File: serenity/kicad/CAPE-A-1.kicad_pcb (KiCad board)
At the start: 4 copper layers, 55 x 35 mm, 25 parts

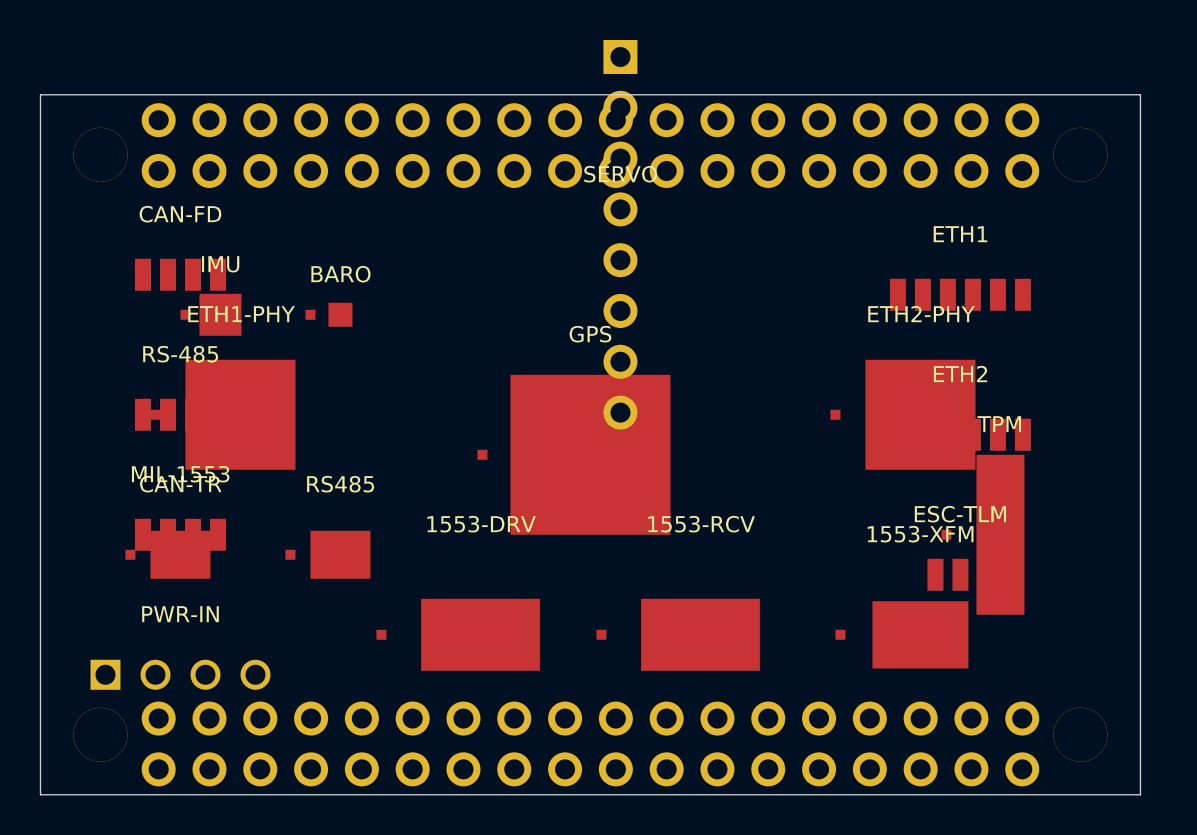
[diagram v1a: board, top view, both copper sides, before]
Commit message: Add back-side RF/storage to CAPE-A-1; add GPIO expansion headers to CAPE-B-1
CAPE-A-1.kicad_pcb:
- Move RFM95W LoRa, WL1837MOD WiFi/BT, ATF16V8BQL CPLD write-blocker,
  W25Q128JV NOR flash, and microSD log slot to B.Cu back side
- Add nets for SPI1 bus (LoRa/NOR), SDIO bus (WiFi), and SD card signals
- Update title comment to list front/back component inventory

CAPE-B-1.kicad_pcb:
- Add 6 × JST-GH 3-pin GPIO expansion connectors (GPIO-A through GPIO-F)
  along bottom edge at 7mm spacing
- Add nets GPIO_EXP_A through GPIO_EXP_F
- Update title comment to mention GPIO expansion

https://claude.ai/code/session_01GniMw4QukTVM7JMzyVjH6p
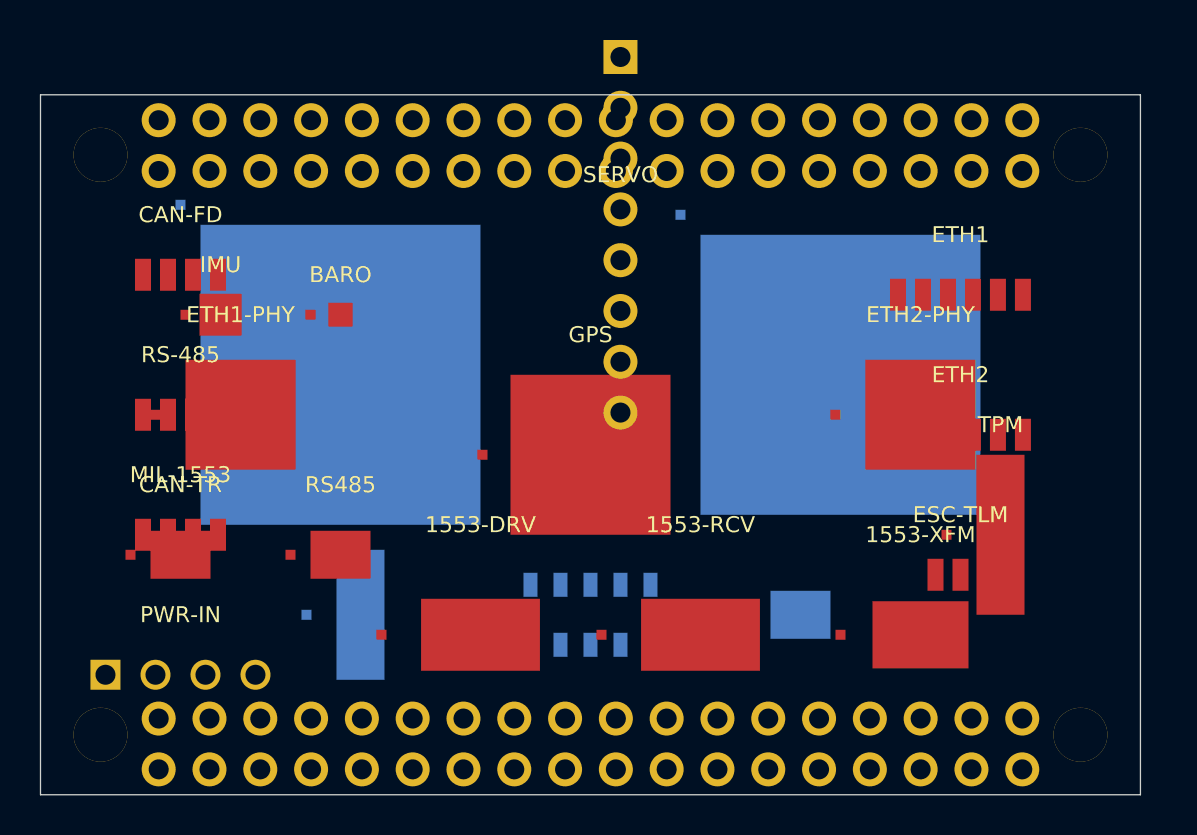
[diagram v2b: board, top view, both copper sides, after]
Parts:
- added J_SD: microSD-Log, microSD_Slot, B.Cu at (148.5, 113.5)
- added LORA: RFM95W, RF_Module, B.Cu at (136.0, 101.5)
- added NOR-FLASH: W25Q128JV, Package, B.Cu at (159.0, 113.5)
- added SD-WB: ATF16V8BQL, Package, B.Cu at (137.0, 113.5)
- added WIFI-BT: WL1837MOD, RF_Module, B.Cu at (161.0, 101.5)
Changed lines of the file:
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@@
     (comment 2 "CC BY 4.0 creativecommons.org/licenses/by/4.0")
     (comment 3 "PocketBeagle 2 Industrial (AM6254) expansion — 55x35mm 4L JLCPCB assembled")
-    (comment 4 "ICM-42688-P IMU | BMP388 Baro | SAM-M10Q GPS | ATA6561 CAN FD | MAX3485E RS-485 | DS26LV31/32 1553 | DP83825I x2 ETH | SLB9670 TPM2")
+    (comment 4 "F: ICM-42688-P IMU | BMP388 Baro | SAM-M10Q GPS | ATA6561 CAN FD | MAX3485E RS-485 | DS26LV31/32 1553 | DP83825I x2 ETH | SLB9670 TPM2 | B: RFM95W LoRa | WL1837MOD WiFi/BT | ATF16V8BQL CPLD | W25Q128JV NOR | microSD log slot")
     (comment 5 "Hull: Peter Farell CC BY 4.0 | Nozzle: BamJr CC BY 4.0 | Firefly/Serenity fan-work, not officially licensed")
   )
@@
   (net 84 "ETH2_RX_P")
   (net 85 "ETH2_RX_N")
+  (net 86 "SPI1_CLK")
+  (net 87 "SPI1_MOSI")
+  (net 88 "SPI1_MISO")
+  (net 89 "SPI1_CS_LORA")
+  (net 90 "SPI1_CS_NOR")
+  (net 91 "LORA_DIO0")
+  (net 92 "LORA_RESETN")
+  (net 93 "SDIO_CLK")
+  (net 94 "SDIO_CMD")
+  (net 95 "SDIO_D0")
+  (net 96 "SDIO_D1")
+  (net 97 "SDIO_D2")
+  (net 98 "SDIO_D3")
+  (net 99 "WL_EN")
+  (net 100 "SD_CLK")
+  (net 101 "SD_CMD")
+  (net 102 "SD_D0")
+  (net 103 "SD_D1")
+  (net 104 "SD_D2")
+  (net 105 "SD_D3")
+  (net 106 "SD_CD")
   (gr_line (start 121 87.5) (end 176 87.5) (layer "Edge.Cuts") (width 0.05))
   (gr_line (start 176 87.5) (end 176 122.5) (layer "Edge.Cuts") (width 0.05))
@@
     (pad "3" thru_hole circle (at 1.25 0) (size 1.5 1.5) (drill 1.0) (layers "*.Cu" "*.Mask"))
     (pad "4" thru_hole circle (at 3.75 0) (size 1.5 1.5) (drill 1.0) (layers "*.Cu" "*.Mask")))
+  (footprint "RF_Module" (layer "B.Cu") (at 136 101.5) (property "Description" "Hope RFM95W LoRa 868/915MHz SPI module 16x17mm — back side, SPI1")
+    (fp_text reference "LORA" (at 0 -10) (layer "B.SilkS")
+      (effects (font (size 0.8 0.8) (thickness 0.15)) (justify mirror)))
+    (fp_text value "RFM95W" (at 0 10) (layer "B.Fab")
+      (effects (font (size 0.8 0.8) (thickness 0.15)) (justify mirror)))
+    (fp_poly (pts (xy -8.0 -8.5) (xy 8.0 -8.5) (xy 8.0 8.5) (xy -8.0 8.5))
+     (layer "B.CrtYd") (width 0.05))
+    (pad "1" smd rect (at -8.0 -8.5) (size 0.5 0.5) (layers "B.Cu" "B.Paste" "B.Mask"))
+    (pad "EP" smd rect (at 0 0) (size 14.0 15.0) (layers "B.Cu" "B.Paste" "B.Mask")))
+  (footprint "RF_Module" (layer "B.Cu") (at 161 101.5) (property "Description" "TI WL1837MOD WiFi 802.11bgn BT4.0 SDIO module 16x16mm — back side, SDIO")
+    (fp_text reference "WIFI-BT" (at 0 -10) (layer "B.SilkS")
+      (effects (font (size 0.8 0.8) (thickness 0.15)) (justify mirror)))
+    (fp_text value "WL1837MOD" (at 0 10) (layer "B.Fab")
+      (effects (font (size 0.8 0.8) (thickness 0.15)) (justify mirror)))
+    (fp_poly (pts (xy -8.0 -8.0) (xy 8.0 -8.0) (xy 8.0 8.0) (xy -8.0 8.0))
+     (layer "B.CrtYd") (width 0.05))
+    (pad "1" smd rect (at -8.0 -8.0) (size 0.5 0.5) (layers "B.Cu" "B.Paste" "B.Mask"))
+    (pad "EP" smd rect (at 0 0) (size 14.0 14.0) (layers "B.Cu" "B.Paste" "B.Mask")))
+  (footprint "Package" (layer "B.Cu") (at 137 113.5) (property "Description" "Microchip ATF16V8BQL GAL CPLD write-blocker for microSD TSSOP-24 — back side")
+    (fp_text reference "SD-WB" (at 0 -4.5) (layer "B.SilkS")
+      (effects (font (size 0.8 0.8) (thickness 0.15)) (justify mirror)))
+    (fp_text value "ATF16V8BQL" (at 0 4.5) (layer "B.Fab")
+      (effects (font (size 0.8 0.8) (thickness 0.15)) (justify mirror)))
+    (fp_poly (pts (xy -2.70 -4.15) (xy 2.70 -4.15) (xy 2.70 4.15) (xy -2.70 4.15))
+     (layer "B.CrtYd") (width 0.05))
+    (pad "1" smd rect (at -2.70 0) (size 0.5 0.5) (layers "B.Cu" "B.Paste" "B.Mask"))
+    (pad "EP" smd rect (at 0 0) (size 2.40 6.50) (layers "B.Cu" "B.Paste" "B.Mask")))
+  (footprint "Package" (layer "B.Cu") (at 159 113.5) (property "Description" "Winbond W25Q128JV 128Mbit NOR flash SPI SOIC-8 — back side, SPI1")
+    (fp_text reference "NOR-FLASH" (at 0 -3.5) (layer "B.SilkS")
+      (effects (font (size 0.8 0.8) (thickness 0.15)) (justify mirror)))
+    (fp_text value "W25Q128JV" (at 0 3.5) (layer "B.Fab")
+      (effects (font (size 0.8 0.8) (thickness 0.15)) (justify mirror)))
+    (fp_poly (pts (xy -2.50 -2.00) (xy 2.50 -2.00) (xy 2.50 2.00) (xy -2.50 2.00))
+     (layer "B.CrtYd") (width 0.05))
+    (pad "1" smd rect (at -2.50 0) (size 0.5 0.5) (layers "B.Cu" "B.Paste" "B.Mask"))
+    (pad "EP" smd rect (at 0 0) (size 3.00 2.40) (layers "B.Cu" "B.Paste" "B.Mask")))
+  (footprint "microSD_Slot" (layer "B.Cu") (at 148.5 113.5) (property "Description" "microSD push-push slot for write-blocked log storage — back side, Molex 503182-1853 or equiv")
+    (fp_text reference "J_SD" (at 0 -4) (layer "B.SilkS")
+      (effects (font (size 0.8 0.8) (thickness 0.15)) (justify mirror)))
+    (fp_text value "microSD-Log" (at 0 4) (layer "B.Fab")
+      (effects (font (size 0.8 0.8) (thickness 0.15)) (justify mirror)))
+    (fp_poly (pts (xy -7.5 -2.0) (xy 7.5 -2.0) (xy 7.5 2.0) (xy -7.5 2.0))
+     (layer "B.CrtYd") (width 0.05))
+    (pad "1" smd rect (at -3.0 -1.5) (size 0.7 1.2) (layers "B.Cu" "B.Paste" "B.Mask"))
+    (pad "2" smd rect (at -1.5 -1.5) (size 0.7 1.2) (layers "B.Cu" "B.Paste" "B.Mask"))
+    (pad "3" smd rect (at 0.0 -1.5) (size 0.7 1.2) (layers "B.Cu" "B.Paste" "B.Mask"))
+    (pad "4" smd rect (at 1.5 -1.5) (size 0.7 1.2) (layers "B.Cu" "B.Paste" "B.Mask"))
+    (pad "5" smd rect (at 3.0 -1.5) (size 0.7 1.2) (layers "B.Cu" "B.Paste" "B.Mask"))
+    (pad "6" smd rect (at -3.0 1.5) (size 0.7 1.2) (layers "B.Cu" "B.Paste" "B.Mask"))
+    (pad "7" smd rect (at -1.5 1.5) (size 0.7 1.2) (layers "B.Cu" "B.Paste" "B.Mask"))
+    (pad "8" smd rect (at 0.0 1.5) (size 0.7 1.2) (layers "B.Cu" "B.Paste" "B.Mask"))
+    (pad "9" smd rect (at 1.5 1.5) (size 0.7 1.2) (layers "B.Cu" "B.Paste" "B.Mask"))
+    (pad "10" smd rect (at 3.0 1.5) (size 0.7 1.2) (layers "B.Cu" "B.Paste" "B.Mask")))
 )

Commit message: Correct placement: flip RF/storage to B.Cu on CAPE-B-1; revert CAPE-A-1
CAPE-B-1.kicad_pcb:
- Flip existing RFM95W LoRa, WL1837MOD WiFi/BT, ATF16V8BQL CPLD
  write-blocker, W25Q128JV NOR flash, and microSD log slot from F.Cu
  to B.Cu (layer, silk, fab, courtyard, pad layers, justify mirror)
- Update title comment to distinguish F/B component inventory

CAPE-A-1.kicad_pcb:
- Revert erroneously added back-side RF/storage footprints and nets
- Restore original title comment (front-only sensor/comms cape)

https://claude.ai/code/session_01GniMw4QukTVM7JMzyVjH6p
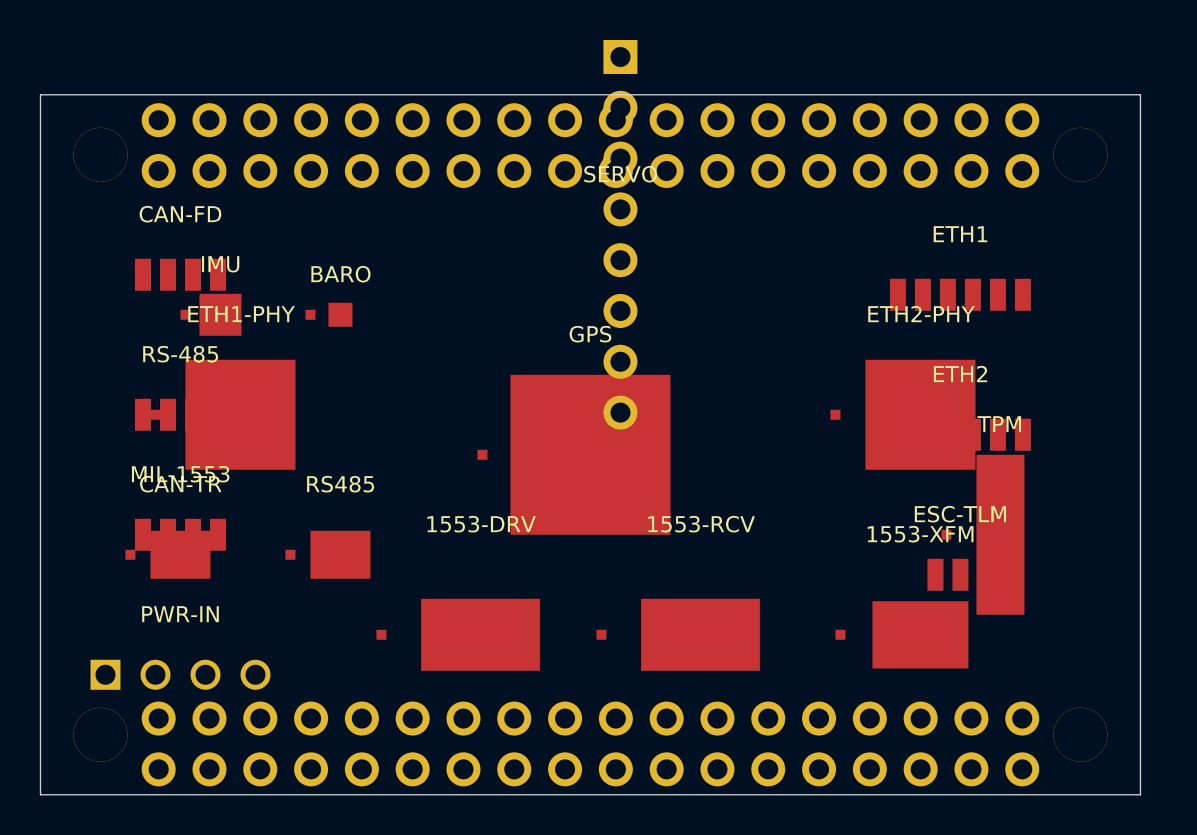
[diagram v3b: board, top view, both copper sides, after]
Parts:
- removed J_SD: microSD-Log, microSD_Slot
- removed LORA: RFM95W, RF_Module
- removed NOR-FLASH: W25Q128JV, Package
- removed SD-WB: ATF16V8BQL, Package
- removed WIFI-BT: WL1837MOD, RF_Module
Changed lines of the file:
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@@
     (comment 2 "CC BY 4.0 creativecommons.org/licenses/by/4.0")
     (comment 3 "PocketBeagle 2 Industrial (AM6254) expansion — 55x35mm 4L JLCPCB assembled")
-    (comment 4 "F: ICM-42688-P IMU | BMP388 Baro | SAM-M10Q GPS | ATA6561 CAN FD | MAX3485E RS-485 | DS26LV31/32 1553 | DP83825I x2 ETH | SLB9670 TPM2 | B: RFM95W LoRa | WL1837MOD WiFi/BT | ATF16V8BQL CPLD | W25Q128JV NOR | microSD log slot")
+    (comment 4 "ICM-42688-P IMU | BMP388 Baro | SAM-M10Q GPS | ATA6561 CAN FD | MAX3485E RS-485 | DS26LV31/32 1553 | DP83825I x2 ETH | SLB9670 TPM2")
     (comment 5 "Hull: Peter Farell CC BY 4.0 | Nozzle: BamJr CC BY 4.0 | Firefly/Serenity fan-work, not officially licensed")
   )
@@
   (net 84 "ETH2_RX_P")
   (net 85 "ETH2_RX_N")
-  (net 86 "SPI1_CLK")
-  (net 87 "SPI1_MOSI")
-  (net 88 "SPI1_MISO")
-  (net 89 "SPI1_CS_LORA")
-  (net 90 "SPI1_CS_NOR")
-  (net 91 "LORA_DIO0")
-  (net 92 "LORA_RESETN")
-  (net 93 "SDIO_CLK")
-  (net 94 "SDIO_CMD")
-  (net 95 "SDIO_D0")
-  (net 96 "SDIO_D1")
-  (net 97 "SDIO_D2")
-  (net 98 "SDIO_D3")
-  (net 99 "WL_EN")
-  (net 100 "SD_CLK")
-  (net 101 "SD_CMD")
-  (net 102 "SD_D0")
-  (net 103 "SD_D1")
-  (net 104 "SD_D2")
-  (net 105 "SD_D3")
-  (net 106 "SD_CD")
   (gr_line (start 121 87.5) (end 176 87.5) (layer "Edge.Cuts") (width 0.05))
   (gr_line (start 176 87.5) (end 176 122.5) (layer "Edge.Cuts") (width 0.05))
@@
     (pad "3" thru_hole circle (at 1.25 0) (size 1.5 1.5) (drill 1.0) (layers "*.Cu" "*.Mask"))
     (pad "4" thru_hole circle (at 3.75 0) (size 1.5 1.5) (drill 1.0) (layers "*.Cu" "*.Mask")))
-  (footprint "RF_Module" (layer "B.Cu") (at 136 101.5) (property "Description" "Hope RFM95W LoRa 868/915MHz SPI module 16x17mm — back side, SPI1")
-    (fp_text reference "LORA" (at 0 -10) (layer "B.SilkS")
-      (effects (font (size 0.8 0.8) (thickness 0.15)) (justify mirror)))
-    (fp_text value "RFM95W" (at 0 10) (layer "B.Fab")
-      (effects (font (size 0.8 0.8) (thickness 0.15)) (justify mirror)))
-    (fp_poly (pts (xy -8.0 -8.5) (xy 8.0 -8.5) (xy 8.0 8.5) (xy -8.0 8.5))
-     (layer "B.CrtYd") (width 0.05))
-    (pad "1" smd rect (at -8.0 -8.5) (size 0.5 0.5) (layers "B.Cu" "B.Paste" "B.Mask"))
-    (pad "EP" smd rect (at 0 0) (size 14.0 15.0) (layers "B.Cu" "B.Paste" "B.Mask")))
-  (footprint "RF_Module" (layer "B.Cu") (at 161 101.5) (property "Description" "TI WL1837MOD WiFi 802.11bgn BT4.0 SDIO module 16x16mm — back side, SDIO")
-    (fp_text reference "WIFI-BT" (at 0 -10) (layer "B.SilkS")
-      (effects (font (size 0.8 0.8) (thickness 0.15)) (justify mirror)))
-    (fp_text value "WL1837MOD" (at 0 10) (layer "B.Fab")
-      (effects (font (size 0.8 0.8) (thickness 0.15)) (justify mirror)))
-    (fp_poly (pts (xy -8.0 -8.0) (xy 8.0 -8.0) (xy 8.0 8.0) (xy -8.0 8.0))
-     (layer "B.CrtYd") (width 0.05))
-    (pad "1" smd rect (at -8.0 -8.0) (size 0.5 0.5) (layers "B.Cu" "B.Paste" "B.Mask"))
-    (pad "EP" smd rect (at 0 0) (size 14.0 14.0) (layers "B.Cu" "B.Paste" "B.Mask")))
-  (footprint "Package" (layer "B.Cu") (at 137 113.5) (property "Description" "Microchip ATF16V8BQL GAL CPLD write-blocker for microSD TSSOP-24 — back side")
-    (fp_text reference "SD-WB" (at 0 -4.5) (layer "B.SilkS")
-      (effects (font (size 0.8 0.8) (thickness 0.15)) (justify mirror)))
-    (fp_text value "ATF16V8BQL" (at 0 4.5) (layer "B.Fab")
-      (effects (font (size 0.8 0.8) (thickness 0.15)) (justify mirror)))
-    (fp_poly (pts (xy -2.70 -4.15) (xy 2.70 -4.15) (xy 2.70 4.15) (xy -2.70 4.15))
-     (layer "B.CrtYd") (width 0.05))
-    (pad "1" smd rect (at -2.70 0) (size 0.5 0.5) (layers "B.Cu" "B.Paste" "B.Mask"))
-    (pad "EP" smd rect (at 0 0) (size 2.40 6.50) (layers "B.Cu" "B.Paste" "B.Mask")))
-  (footprint "Package" (layer "B.Cu") (at 159 113.5) (property "Description" "Winbond W25Q128JV 128Mbit NOR flash SPI SOIC-8 — back side, SPI1")
-    (fp_text reference "NOR-FLASH" (at 0 -3.5) (layer "B.SilkS")
-      (effects (font (size 0.8 0.8) (thickness 0.15)) (justify mirror)))
-    (fp_text value "W25Q128JV" (at 0 3.5) (layer "B.Fab")
-      (effects (font (size 0.8 0.8) (thickness 0.15)) (justify mirror)))
-    (fp_poly (pts (xy -2.50 -2.00) (xy 2.50 -2.00) (xy 2.50 2.00) (xy -2.50 2.00))
-     (layer "B.CrtYd") (width 0.05))
-    (pad "1" smd rect (at -2.50 0) (size 0.5 0.5) (layers "B.Cu" "B.Paste" "B.Mask"))
-    (pad "EP" smd rect (at 0 0) (size 3.00 2.40) (layers "B.Cu" "B.Paste" "B.Mask")))
-  (footprint "microSD_Slot" (layer "B.Cu") (at 148.5 113.5) (property "Description" "microSD push-push slot for write-blocked log storage — back side, Molex 503182-1853 or equiv")
-    (fp_text reference "J_SD" (at 0 -4) (layer "B.SilkS")
-      (effects (font (size 0.8 0.8) (thickness 0.15)) (justify mirror)))
-    (fp_text value "microSD-Log" (at 0 4) (layer "B.Fab")
-      (effects (font (size 0.8 0.8) (thickness 0.15)) (justify mirror)))
-    (fp_poly (pts (xy -7.5 -2.0) (xy 7.5 -2.0) (xy 7.5 2.0) (xy -7.5 2.0))
-     (layer "B.CrtYd") (width 0.05))
-    (pad "1" smd rect (at -3.0 -1.5) (size 0.7 1.2) (layers "B.Cu" "B.Paste" "B.Mask"))
-    (pad "2" smd rect (at -1.5 -1.5) (size 0.7 1.2) (layers "B.Cu" "B.Paste" "B.Mask"))
-    (pad "3" smd rect (at 0.0 -1.5) (size 0.7 1.2) (layers "B.Cu" "B.Paste" "B.Mask"))
-    (pad "4" smd rect (at 1.5 -1.5) (size 0.7 1.2) (layers "B.Cu" "B.Paste" "B.Mask"))
-    (pad "5" smd rect (at 3.0 -1.5) (size 0.7 1.2) (layers "B.Cu" "B.Paste" "B.Mask"))
-    (pad "6" smd rect (at -3.0 1.5) (size 0.7 1.2) (layers "B.Cu" "B.Paste" "B.Mask"))
-    (pad "7" smd rect (at -1.5 1.5) (size 0.7 1.2) (layers "B.Cu" "B.Paste" "B.Mask"))
-    (pad "8" smd rect (at 0.0 1.5) (size 0.7 1.2) (layers "B.Cu" "B.Paste" "B.Mask"))
-    (pad "9" smd rect (at 1.5 1.5) (size 0.7 1.2) (layers "B.Cu" "B.Paste" "B.Mask"))
-    (pad "10" smd rect (at 3.0 1.5) (size 0.7 1.2) (layers "B.Cu" "B.Paste" "B.Mask")))
 )
